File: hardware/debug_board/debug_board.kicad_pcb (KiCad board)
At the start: 4 copper layers, 58.3 x 59.6 mm, 6 parts, among them CN1 Conn_05x02_Female, J11 Conn_02x05_Counter_Clockwise, J13 Conn_02x16_Counter_Clockwise, J15 Conn_02x16_Counter_Clockwise, J5 Conn_02x03_Odd_Even, J6 Conn_01x32_MountingPin

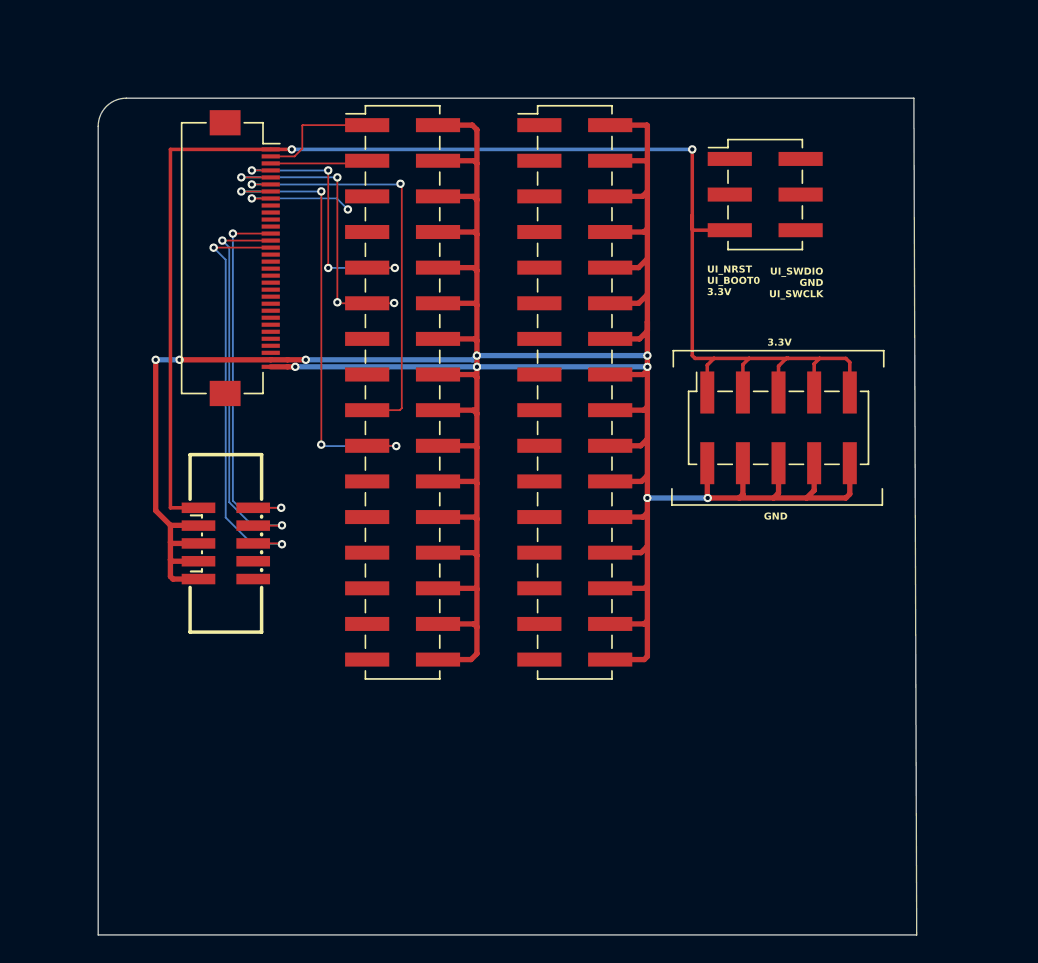
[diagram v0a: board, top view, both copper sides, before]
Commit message: Created debug board
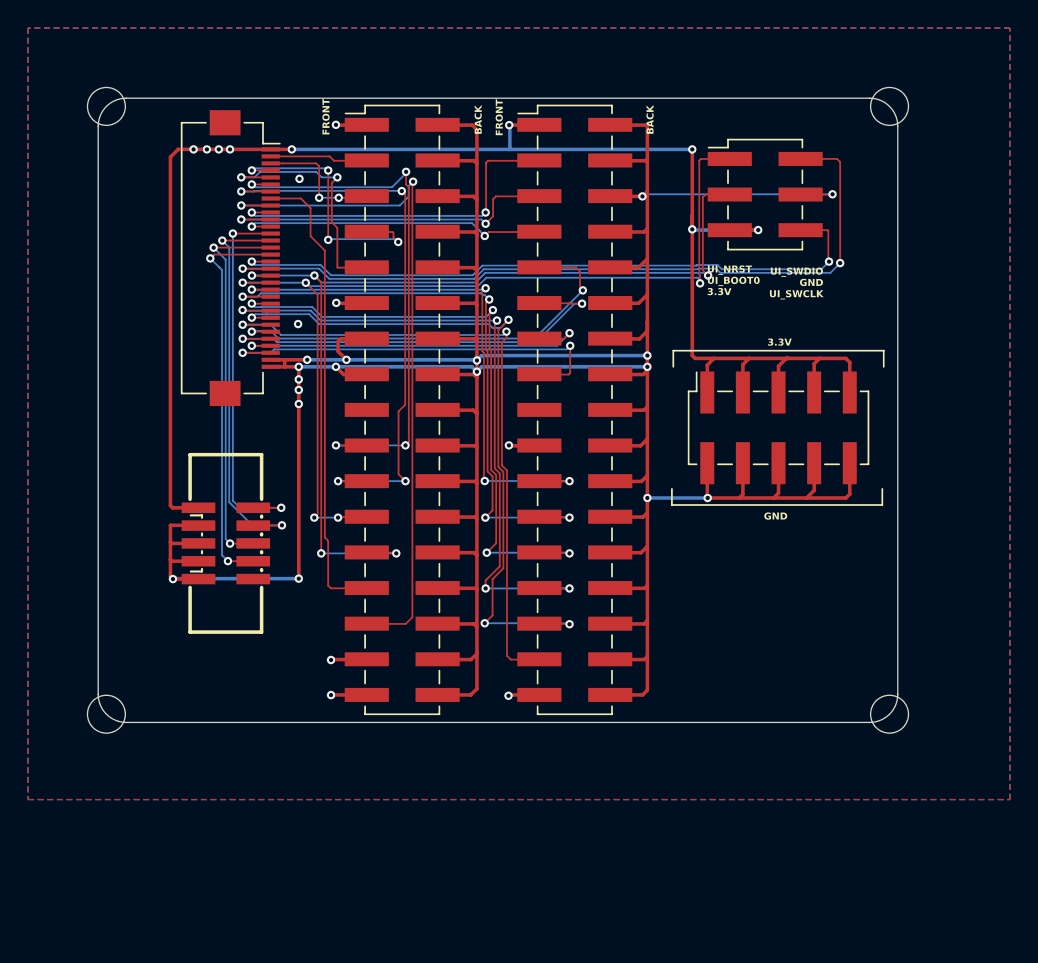
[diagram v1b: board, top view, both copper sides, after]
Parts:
- added H1: MountingHole, MountingHole:MountingHole_2.7mm_M2.5, F.Cu at (42.5, 37.4)
- added H2: MountingHole, MountingHole:MountingHole_2.7mm_M2.5, F.Cu at (42.5, 80.8)
- added H3: MountingHole, MountingHole:MountingHole_2.7mm_M2.5, F.Cu at (98.3, 37.4)
- added H4: MountingHole, MountingHole:MountingHole_2.7mm_M2.5, F.Cu at (98.3, 80.8)
- J13, J15: value Conn_02x16_Counter_Clockwise -> Conn_02x17_Counter_Clockwise; footprint Connector_PinHeader_2.54mm:PinHeader_2x16_P2.54mm_Vertical_SMD -> Connector_PinHeader_2.54mm:PinHeader_2x17_P2.54mm_Vertical_SMD
- moved J13 1.25 mm to (63.5, 59.1)
- moved J15 1.25 mm to (75.8, 59.1)
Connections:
- J13 pad 1: /USB_TX1_MGMT -> +3.3V
- J13 pad 11: /NET_RX1_MGMT -> GND
- J13 pad 13: /NET_BOOT -> GND
- J13 pad 15: /NET_NRST -> GND
- J13 pad 17: /UI_TX1_MGMT -> unconnected-(J13-Pin_17-Pad17)
- J13 pad 19: /UI_RX1_MGMT -> /UI_TX1_MGMT
- J13 pad 21: /UI_NRST -> /UI_RX1_MGMT
- J13 pad 23: /UI_BOOT0 -> /UI_NRST
- J13 pad 25: /UI_TX2_NET -> /UI_BOOT0
- J13 pad 27: /UI_RX2_NET -> /UI_TX2_NET
- J13 pad 29: /UI_RTS2_NET -> /UI_RX2_NET
- J13 pad 3: /USB_RX1_MGMT -> /USB_TX1_MGMT
- J13 pad 31: /UI_CTS2_NET -> GND
- J13 pad 5: /USB_RTS_MGMT -> /USB_RX1_MGMT
- J13 pad 7: /USB_DTR_MGMT -> /NET_TX1_MGMT
- J13 pad 9: /NET_TX1_MGMT -> /NET_RX1_MGMT
- J15 pad 1: /SPI1_MOSI -> +3.3V
- J15 pad 11: /I2S_DACDAT -> /I2S_ADCDAT
- J15 pad 13: /I2S_ADCDAT -> /I2S_BCLK
- J15 pad 15: /I2S_BCLK -> /I2S_DACLRC
- J15 pad 17: /I2S_DACLRC -> unconnected-(J15-Pin_17-Pad17)
- J15 pad 19: /MGMT_DEBUG_1 -> GND
- J15 pad 21: /MGMT_DEBUG_2 -> /MGMT_DEBUG_1
- J15 pad 23: /UI_DEBUG_1 -> /MGMT_DEBUG_2
- J15 pad 25: /UI_DEBUG_2 -> /UI_DEBUG_1
- J15 pad 27: /NET_DEBUG_1 -> /UI_DEBUG_2
- J15 pad 29: /NET_DEBUG_2 -> /NET_DEBUG_1
- J15 pad 31: unconnected-(J15-Pin_31-Pad31) -> /NET_DEBUG_2
- J15 pad 5: /SPI1_MISO -> /SPI1_MOSI
- J15 pad 7: /I2C1_SDA -> /SPI1_MISO
- J15 pad 9: /I2C1_SCL -> /I2S_DACDAT
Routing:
- net /UI_BOOT0: track 0.00 -> 69.7 mm, vias 0 -> 5
- net /UI_NRST: track 0.00 -> 67.2 mm, vias 0 -> 5
- net /UI_SWDIO: track 0.00 -> 55.7 mm, vias 0 -> 2
- net /NET_DEBUG_1: track 0.00 -> 51.3 mm, vias 0 -> 4
- net /UI_RX2_NET: track 0.00 -> 50.0 mm, vias 0 -> 2
- net GND: track 279.4 -> 328.5 mm, vias 10 -> 24
- net /UI_DEBUG_2: track 0.00 -> 48.3 mm, vias 0 -> 4
- net /UI_SWCLK: track 0.00 -> 47.8 mm, vias 0 -> 2
- net /NET_DEBUG_2: track 0.00 -> 46.9 mm, vias 0 -> 2
- net /UI_DEBUG_1: track 0.00 -> 45.1 mm, vias 0 -> 4
- net /MGMT_DEBUG_2: track 0.00 -> 44.1 mm, vias 0 -> 4
- net /MGMT_DEBUG_1: track 0.00 -> 40.2 mm, vias 0 -> 4
- net /I2S_DACDAT: track 0.00 -> 31.1 mm, vias 0 -> 2
- net /I2S_ADCDAT: track 0.00 -> 30.5 mm, vias 0 -> 2
- net /I2S_DACLRC: track 0.00 -> 29.7 mm, vias 0 -> 2
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- added copper zone on In2.Cu, net +3.3V
- added copper zone on B.Cu, net GND
- added copper zone on F.Cu, net GND
- added copper zone on In1.Cu, net GND
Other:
- board size 58.3 x 59.6 mm -> 57 x 44.5 mm
- board text added: "BACK"
- board text added: "FRONT"
